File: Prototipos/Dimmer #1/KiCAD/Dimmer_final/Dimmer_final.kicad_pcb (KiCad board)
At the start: 2 copper layers, 50 x 100 mm, 32 parts, among them J2 Conn_01x02, K1 SRD-05VDC-SL-C, M5_BotL MountingHole_5.3mm_M5, M5_BotR MountingHole_5.3mm_M5, M5_TopL MountingHole_5.3mm_M5, M5_TopR MountingHole_5.3mm_M5, Q1 BC548B, Q2 BT137, U1 MOC3021M, U2 EL817

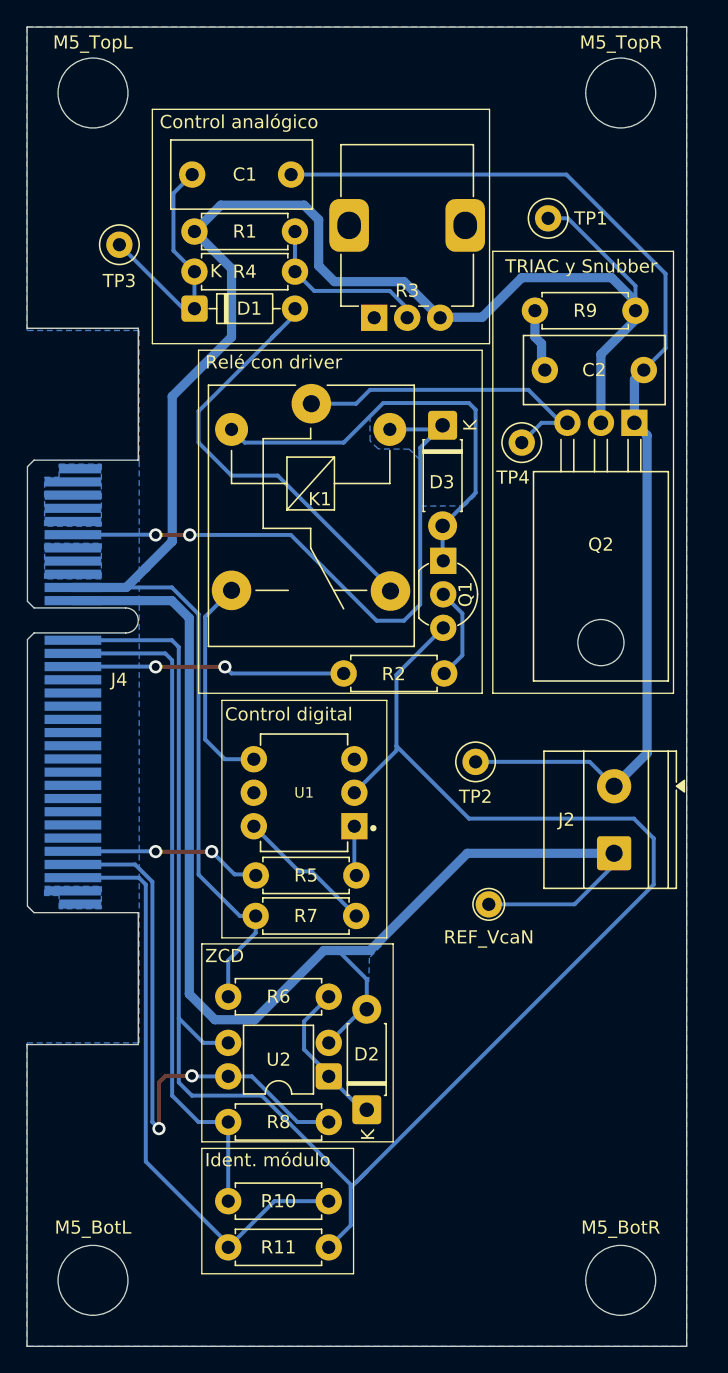
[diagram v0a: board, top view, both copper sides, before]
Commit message: Primeras modificaciones para constraints JLCPCB
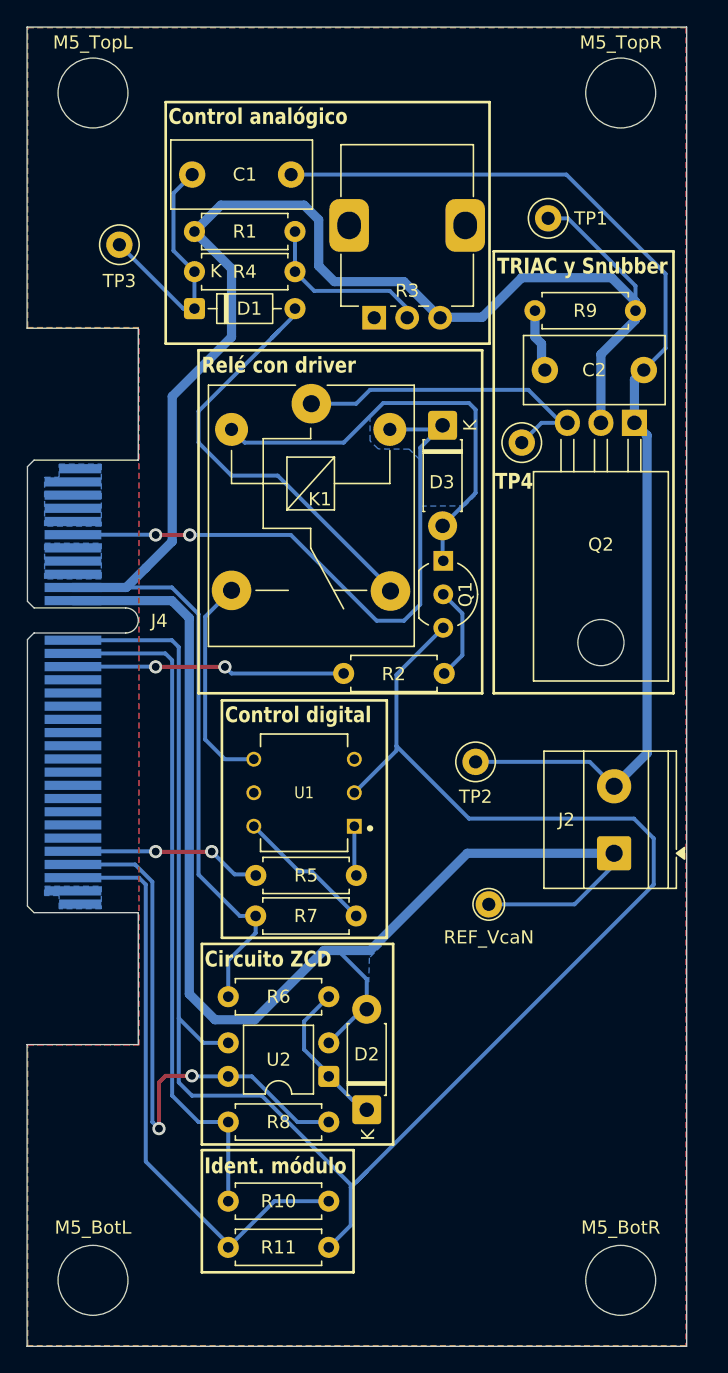
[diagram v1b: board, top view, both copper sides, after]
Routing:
- added copper zone on F.Cu, net AGND
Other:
- rule pad_to_mask_clearance: 0 -> 0.045
- board text added: "Circuito ZCD"
- board text removed: "ZCD"

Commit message: Reversionado dimmer para fabricación industrial
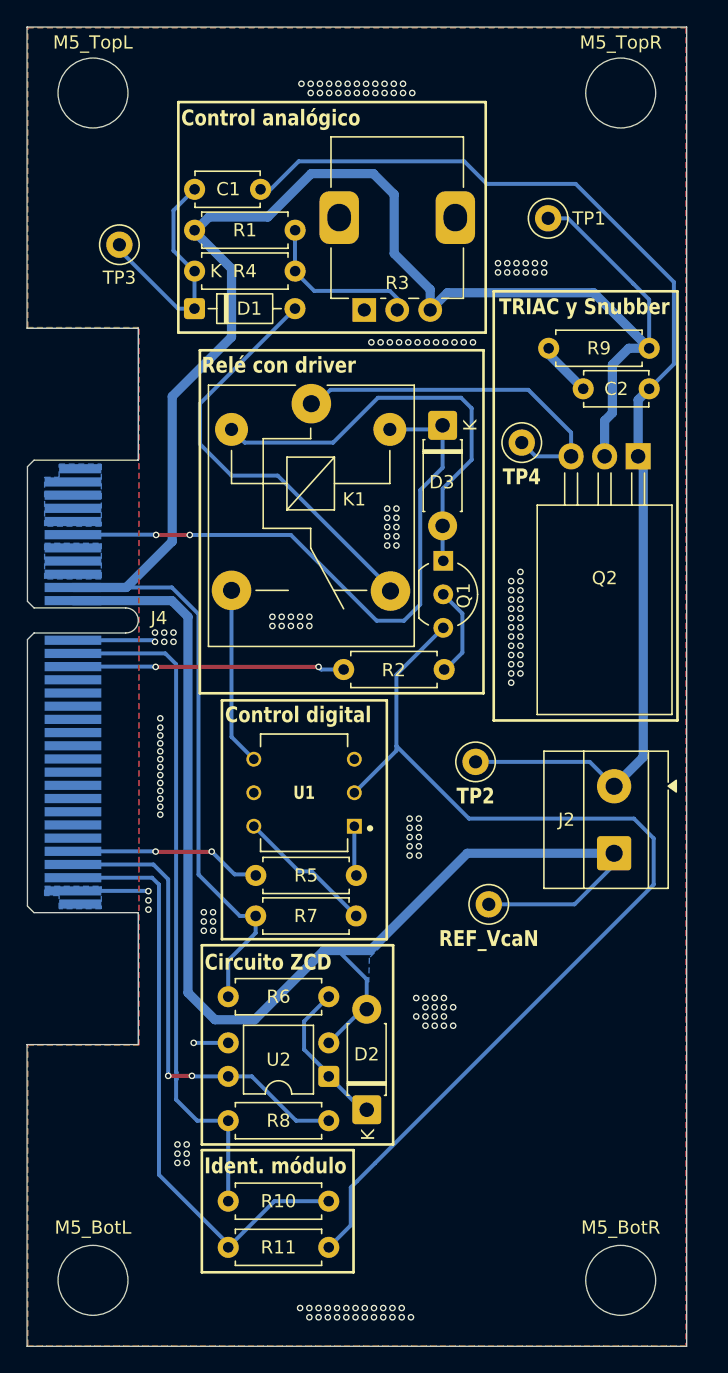
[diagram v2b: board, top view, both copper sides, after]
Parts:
- C1, C2: footprint Capacitor_THT:C_Disc_D10.5mm_W5.0mm_P7.50mm -> Capacitor_THT:C_Disc_D4.7mm_W2.5mm_P5.00mm
- REF_VcaN: value TestPoint_THTPad_D2.0mm_Drill1.0mm -> TestPoint_Loop_D1.80mm_Drill1.0mm_Beaded; footprint TestPoint:TestPoint_THTPad_D2.0mm_Drill1.0mm -> TestPoint:TestPoint_Loop_D1.80mm_Drill1.0mm_Beaded
- moved C2 3.24 mm to (134.2, 72.4)
- moved R9 3.03 mm to (139.2, 69.3)
- moved Q2 2.56 mm to (138.3, 77.5)
- moved C1 1.13 mm to (104.7, 57.3)
- moved R3 0.96 mm to (117.6, 66.4)
- moved R2 0.30 mm to (116.0, 93.7)
- moved R1 0.10 mm to (104.7, 60.4)
- moved R8 0.10 mm to (107.2, 127.9)
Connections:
- R3 pad MP: (no net) -> AGND
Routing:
- net AGND: track 142.2 -> 93.4 mm, vias 0 -> 177
- net UC_PHASE: track 43.5 -> 36.2 mm
- net 48Vca_L: track 137.9 -> 145.0 mm
- net LOAD_L: track 84.5 -> 87.8 mm
- net Net-(K1-Pad3): track 16.4 -> 13.5 mm
- net Net-(Q2-G): track 25.0 -> 27.4 mm
- net Net-(D1-K): track 19.1 -> 18.2 mm
- net Net-(D1-A): track 33.3 -> 32.4 mm
- net Net-(C2-Pad1): track 4.81 -> 4.16 mm
- net Net-(R1-Pad2): track 13.4 -> 12.8 mm
- net IDENT_V: track 44.9 -> 45.5 mm
- removed copper zone on B.Cu, net 5Vcc
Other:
- rule pad_to_mask_clearance: 0.045 -> 0

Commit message: Correcciones Alejo
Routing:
- net AGND: track 93.4 -> 37.6 mm, vias 177 -> 178
- net 5Vcc: track 48.0 -> 31.5 mm
- net 48Vca_L: track 145.0 -> 143.2 mm
